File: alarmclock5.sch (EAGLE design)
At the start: 37 parts, among them X1 MKDSN1,5/2-5,08, X2 MKDSN1,5/2-5,08, X3 MKDSN1,5/2-5,08, X4 MKDSN1,5/2-5,08, X5 MKDSN1,5/2-5,08

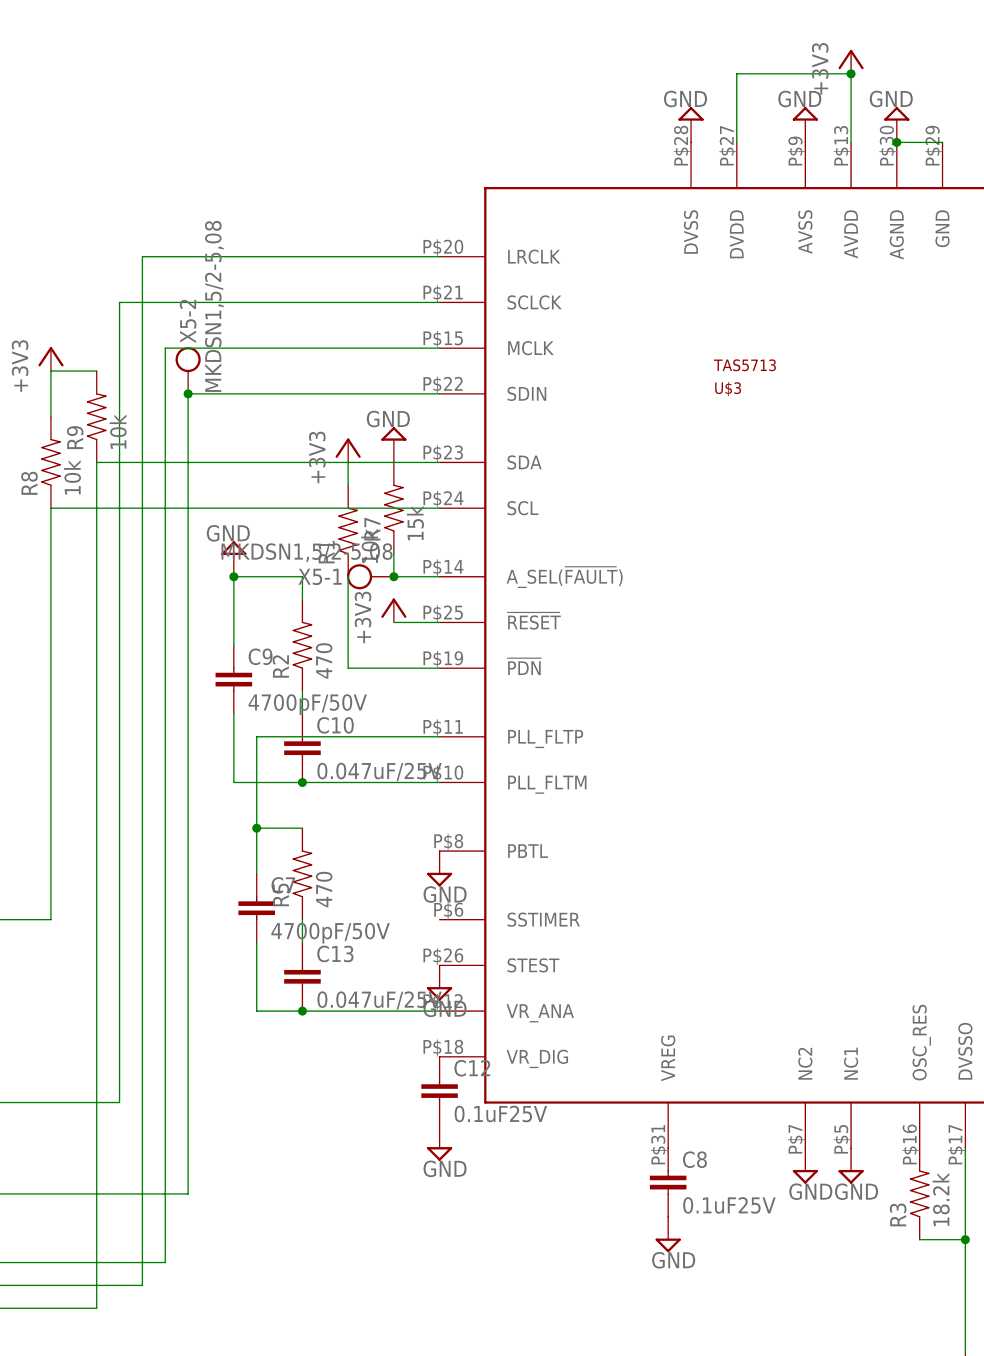
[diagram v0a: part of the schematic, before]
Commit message: add a reset pin
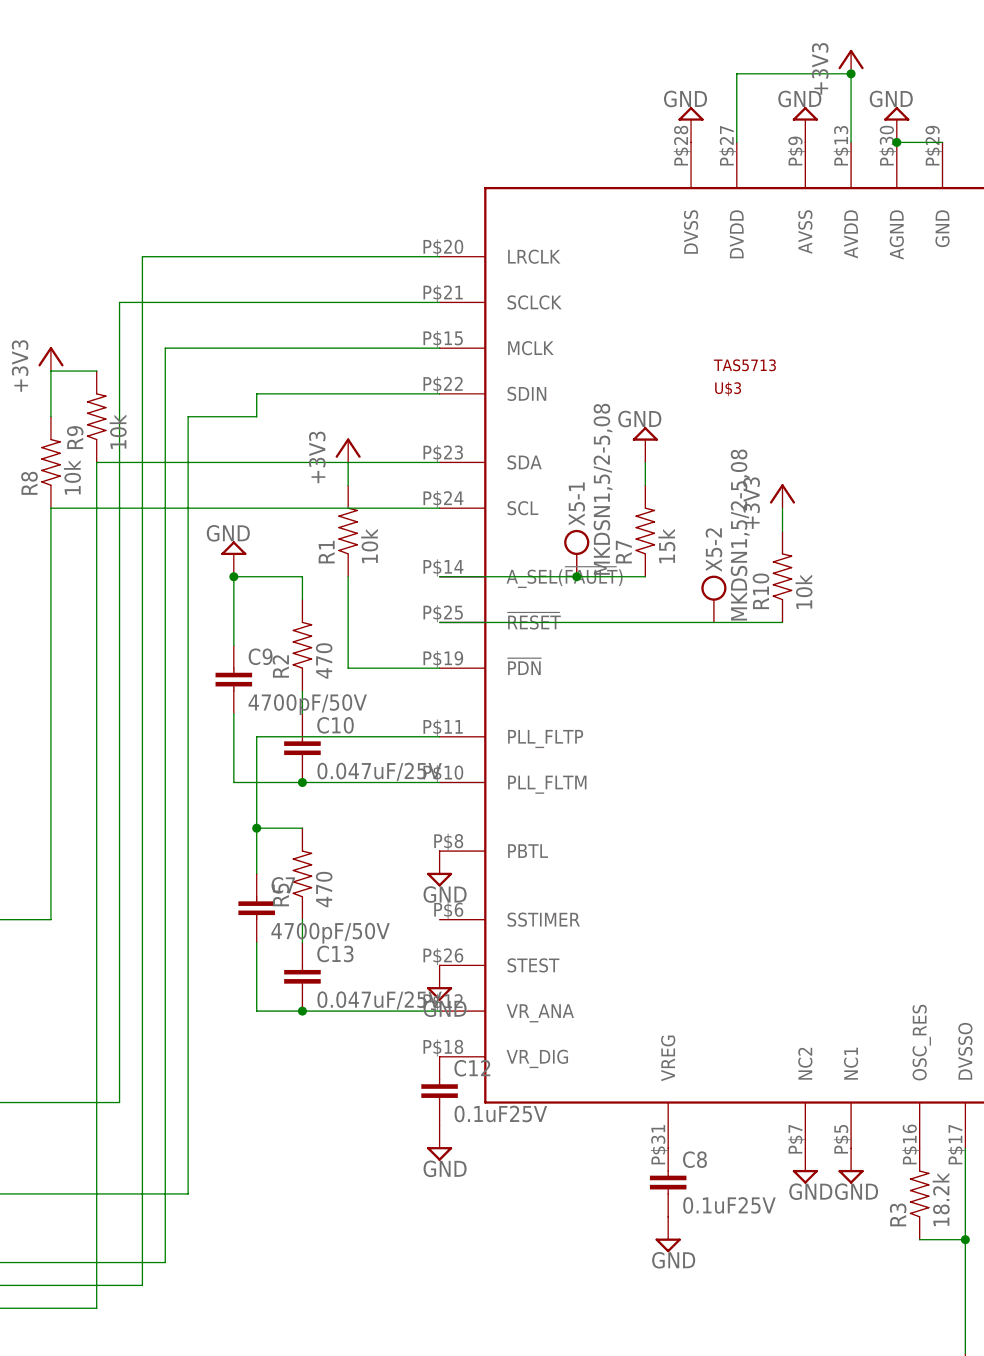
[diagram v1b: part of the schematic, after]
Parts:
- added R10: 10k, SparkFun-Passives:RESISTOR0603-RES
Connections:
- new net N$37: R10.1, U$3.!RESET!, X5-2.KL
- net +3V3: now also R10.2; no longer U$3.!RESET!
- net N$1: no longer X5-2.KL
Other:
- moved on the sheet: R7, X5-1, X5-2
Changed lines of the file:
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@@
 <part name="+3V8" library="supply1" deviceset="+3V3" device=""/>
 <part name="X5" library="con-phoenix-508" deviceset="MKDSN1,5/2-5,08" device=""/>
+<part name="R10" library="SparkFun-Passives" deviceset="RESISTOR" device="0603-RES" value="10k"/>
 </parts>
 <sheets>
@@
 <instance part="SUPPLY16" gate="GND" x="20.32" y="-15.24"/>
 <instance part="SUPPLY17" gate="GND" x="20.32" y="5.08"/>
-<instance part="SUPPLY19" gate="GND" x="71.12" y="5.08" rot="R180"/>
+<instance part="SUPPLY19" gate="GND" x="99.06" y="5.08" rot="R180"/>
 <instance part="SUPPLY20" gate="GND" x="76.2" y="-43.18"/>
 <instance part="SUPPLY21" gate="GND" x="76.2" y="-55.88"/>
@@
 <instance part="SUPPLY25" gate="GND" x="121.92" y="-76.2"/>
 <instance part="SUPPLY26" gate="GND" x="134.62" y="-99.06"/>
-<instance part="+3V4" gate="G$1" x="71.12" y="-12.7"/>
+<instance part="+3V4" gate="G$1" x="114.3" y="0"/>
 <instance part="X3" gate="-1" x="-68.58" y="-7.62" rot="R180"/>
 <instance part="X3" gate="-2" x="-68.58" y="-12.7" rot="R180"/>
@@
 <instance part="+3V7" gate="G$1" x="-60.96" y="53.34"/>
 <instance part="SUPPLY29" gate="GND" x="-60.96" y="22.86"/>
-<instance part="R7" gate="G$1" x="71.12" y="-2.54" rot="R90"/>
+<instance part="R7" gate="G$1" x="99.06" y="-5.08" rot="R90"/>
 <instance part="R8" gate="G$1" x="33.02" y="2.54" rot="R90"/>
 <instance part="R9" gate="G$1" x="38.1" y="7.62" rot="R90"/>
 <instance part="+3V8" gate="G$1" x="33.02" y="15.24"/>
-<instance part="X5" gate="-1" x="68.58" y="-10.16" rot="R180"/>
-<instance part="X5" gate="-2" x="48.26" y="12.7" rot="R90"/>
+<instance part="X5" gate="-1" x="91.44" y="-7.62" rot="R90"/>
+<instance part="X5" gate="-2" x="106.68" y="-12.7" rot="R90"/>
+<instance part="R10" gate="G$1" x="114.3" y="-10.16" rot="R90"/>
 </instances>
 <busses>
@@
 <pinref part="R7" gate="G$1" pin="2"/>
 <pinref part="SUPPLY19" gate="GND" pin="GND"/>
+<wire x1="99.06" y1="0" x2="99.06" y2="2.54" width="0.1524" layer="91"/>
 </segment>
 </net>
@@
 <pinref part="U$5" gate="G$1" pin="I2S0_DO"/>
 <wire x1="20.32" y1="-78.74" x2="48.26" y2="-78.74" width="0.1524" layer="91"/>
-<wire x1="48.26" y1="-78.74" x2="48.26" y2="10.16" width="0.1524" layer="91"/>
+<wire x1="48.26" y1="-78.74" x2="48.26" y2="7.62" width="0.1524" layer="91"/>
 <pinref part="U$3" gate="G$1" pin="SDIN"/>
-<wire x1="48.26" y1="10.16" x2="76.2" y2="10.16" width="0.1524" layer="91"/>
-<pinref part="X5" gate="-2" pin="KL"/>
-<junction x="48.26" y="10.16"/>
+<wire x1="55.88" y1="10.16" x2="76.2" y2="10.16" width="0.1524" layer="91"/>
+<wire x1="55.88" y1="10.16" x2="55.88" y2="7.62" width="0.1524" layer="91"/>
+<wire x1="55.88" y1="7.62" x2="48.26" y2="7.62" width="0.1524" layer="91"/>
 </segment>
 </net>
@@
 </segment>
 <segment>
-<pinref part="U$3" gate="G$1" pin="!RESET!"/>
-<wire x1="71.12" y1="-15.24" x2="76.2" y2="-15.24" width="0.1524" layer="91"/>
-<pinref part="+3V4" gate="G$1" pin="+3V3"/>
-</segment>
-<segment>
 <pinref part="R6" gate="G$1" pin="2"/>
 <pinref part="+3V6" gate="G$1" pin="+3V3"/>
@@
 <wire x1="38.1" y1="12.7" x2="33.02" y2="12.7" width="0.1524" layer="91"/>
 <wire x1="33.02" y1="12.7" x2="33.02" y2="7.62" width="0.1524" layer="91"/>
+</segment>
+<segment>
+<pinref part="R10" gate="G$1" pin="2"/>
+<pinref part="+3V4" gate="G$1" pin="+3V3"/>
+<wire x1="114.3" y1="-5.08" x2="114.3" y2="-2.54" width="0.1524" layer="91"/>
 </segment>
 </net>
@@
 <segment>
 <pinref part="R7" gate="G$1" pin="1"/>
-<wire x1="71.12" y1="-7.62" x2="71.12" y2="-10.16" width="0.1524" layer="91"/>
+<wire x1="99.06" y1="-10.16" x2="91.44" y2="-10.16" width="0.1524" layer="91"/>
 <pinref part="U$3" gate="G$1" pin="A_SEL(!FAULT!)"/>
-<wire x1="71.12" y1="-10.16" x2="76.2" y2="-10.16" width="0.1524" layer="91"/>
+<wire x1="91.44" y1="-10.16" x2="76.2" y2="-10.16" width="0.1524" layer="91"/>
 <pinref part="X5" gate="-1" pin="KL"/>
-<junction x="71.12" y="-10.16"/>
+<junction x="91.44" y="-10.16"/>
 </segment>
 </net>
@@
 </segment>
 </net>
+<net name="N$37" class="0">
+<segment>
+<pinref part="U$3" gate="G$1" pin="!RESET!"/>
+<pinref part="X5" gate="-2" pin="KL"/>
+<wire x1="106.68" y1="-15.24" x2="76.2" y2="-15.24" width="0.1524" layer="91"/>
+<pinref part="R10" gate="G$1" pin="1"/>
+<wire x1="106.68" y1="-15.24" x2="114.3" y2="-15.24" width="0.1524" layer="91"/>
+</segment>
+</net>
